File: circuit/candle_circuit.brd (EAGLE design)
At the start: 23 parts, among them IC1 TINY10P, SW1 KMR2, SW2 KMR2

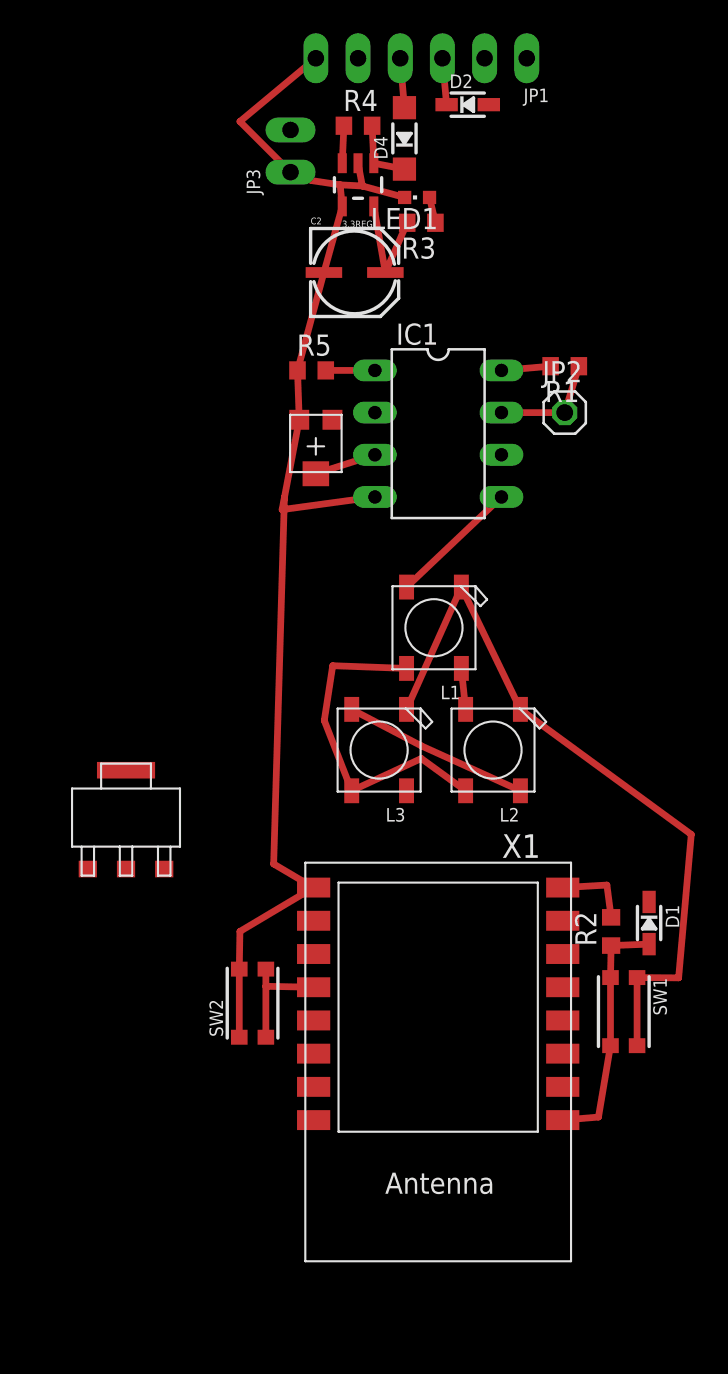
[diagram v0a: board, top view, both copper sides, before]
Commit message: Updates to circuit, client
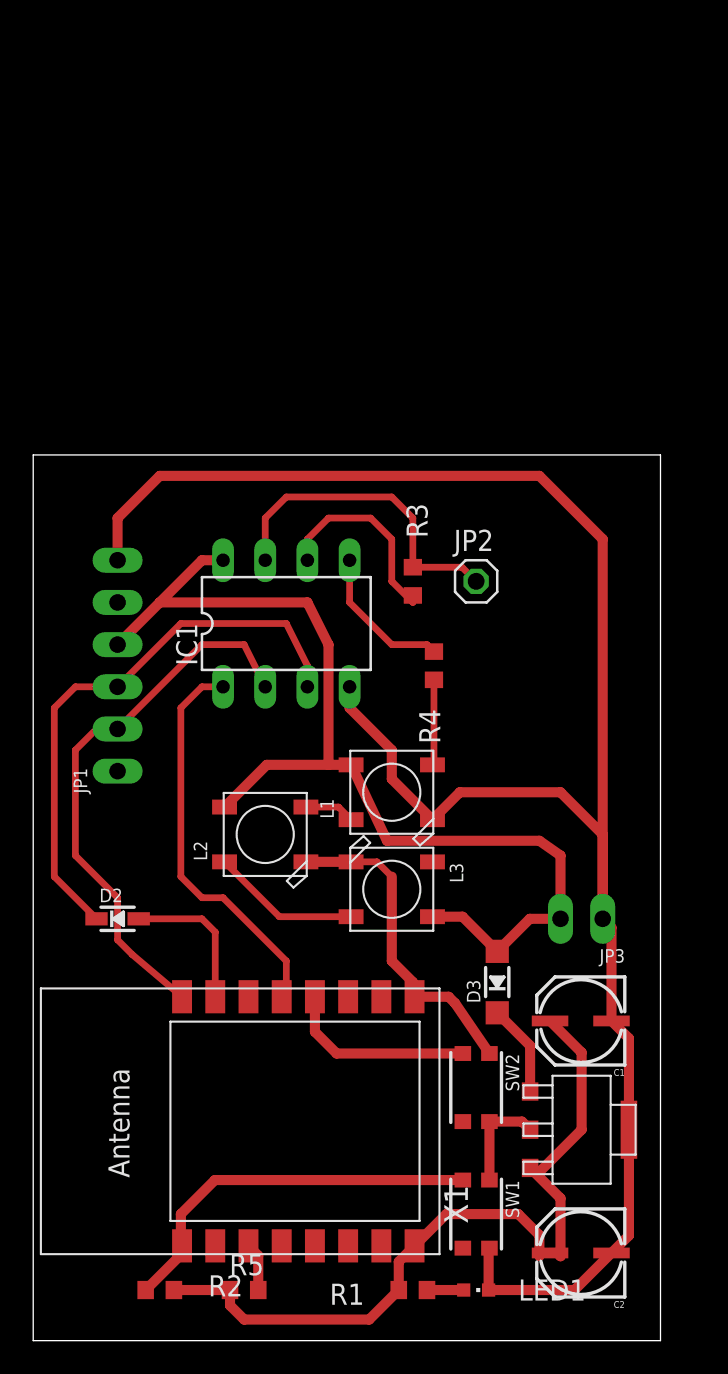
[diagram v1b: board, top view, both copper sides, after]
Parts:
- removed 3.3REG: 3.3V/150mA, SparkFun-PowerIC:SOT23-5
- removed D1: 1n4148, microbuilder:SOD-323
- removed D4: MBR120, microbuilder:SOD-123
- removed U$4: POTENTIOMETER-SMD-P3W, ITP_Lab:POTENTIOMETER-SMD-P3W
- added C1: 0.1uF, SparkFun-Capacitors:PANASONIC_C
- added D3: MBR120, microbuilder:SOD-123
- C2: value (none) -> 0.1uF
- JP1: value (none) -> FTDI
- JP3: value (none) -> POWER
- LED1: value (none) -> RED
- R1: value 47K -> 10k
- R3: value 10k -> 1M
- R4: value 10k -> 470
- X1: value (none) -> ESP-12
- moved LED1 65.9 mm to (26.7, 1.78), turned to 270 degrees
- moved C2 61.0 mm to (33.0, 3.81), turned to 180 degrees
- moved R1 56.4 mm to (22.9, 1.78)
- moved R5 55.5 mm to (12.7, 1.78)
- moved D2 53.4 mm to (5.08, 24.1)
- moved JP3 49.4 mm to (33.0, 24.1), turned to 180 degrees
- moved JP1 40.9 mm to (5.08, 39.4), turned to 90 degrees
- moved R2 34.7 mm to (7.62, 1.78), turned to 0 degrees
- moved U$1 33.3 mm to (33.0, 11.4), turned to 270 degrees
- moved R4 32.8 mm to (24.1, 39.4), turned to 90 degrees
- moved R3 21.6 mm to (22.9, 44.5), turned to 270 degrees
- moved SW1 15.1 mm to (26.7, 6.35)
- moved IC1 14.6 mm to (15.2, 41.9), turned to 0 degrees
- moved L2 14.6 mm to (14.0, 29.2), turned to 180 degrees
- moved SW2 14.4 mm to (26.7, 14.0), turned to 270 degrees
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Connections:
- removed net N$10: 3.3REG.1, D4.C, R4.2
- removed net N$9: 3.3REG.3, R4.1
- removed net RESET_5V: D1.C
- removed net TRIMMER: IC1.3, U$4.2
- new net CH_PD: R5.2, X1.3
- new net N$5: D3.C, U$1.1
- new net N$7: IC1.6, R3.2
- new net N$8: L1.4-DIN, R4.1
- net +3V3: now also C1.+, R5.1, U$1.3; no longer 3.3REG.5, IC1.8, R3.2, U$4.1
- net GND: now also C1.-, U$1.2, U$1.4; no longer 3.3REG.2, 3.3REG.4, R5.1, U$4.3
- net GPIO15: now also X1.13; no longer R5.2, X1.10
- net N$1: now also R4.2; no longer L1.4-DIN
- net N$4: now also R1.1; no longer R3.1
- net RESET: no longer D1.A
- net RXD: no longer IC1.6
- net RXD_5V: now also IC1.3
- net SENSOR: now also R3.1; no longer R1.1
- net V+: now also D3.A, IC1.8; no longer D4.A
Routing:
- net V+: track 23.2 -> 65.1 mm
- net TXD: track 0.00 -> 33.3 mm
- net +3V3: track 14.9 -> 46.4 mm
- net RXD_5V: track 2.81 -> 33.9 mm
- net GPIO15: track 2.96 -> 23.9 mm
- net GND: track 125.1 -> 145.0 mm
- net SENSOR: track 6.73 -> 19.6 mm
- net N$7: track 0.00 -> 12.2 mm
- net RESET: track 14.8 -> 23.8 mm
- net RXD: track 0.00 -> 8.83 mm
- net N$5: track 0.00 -> 5.56 mm
- net N$8: track 0.00 -> 5.16 mm
- net GPIO0: track 6.98 -> 11.6 mm
- net N$10: track 4.14 -> 0.00 mm
- net TRIMMER: track 3.73 -> 0.00 mm
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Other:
- board outline added: 37.8 x 53.3 mm
